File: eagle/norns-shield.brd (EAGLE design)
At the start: 85.1 x 80 mm, 80 parts, among them J1 TRS-IN, J2 TRS-OUT, J3 ISP-ROW, Q1 ASFL-12.288mhz, SW1 PVA1, SW2 PVA1, SW3 PVA1, U1 CS4270, X1 RASPI_BOARD_B+#_E3

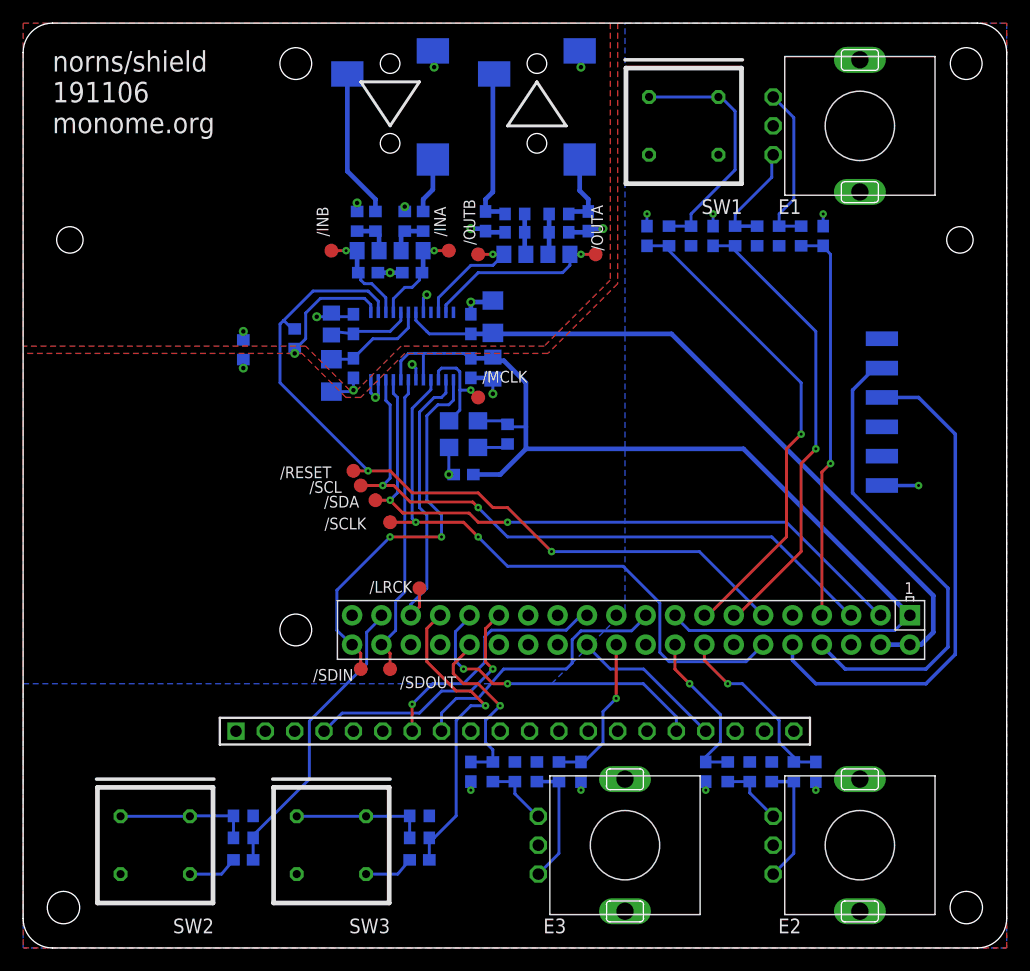
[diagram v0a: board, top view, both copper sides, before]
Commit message: Flip Tip and Ring on IO jacks.
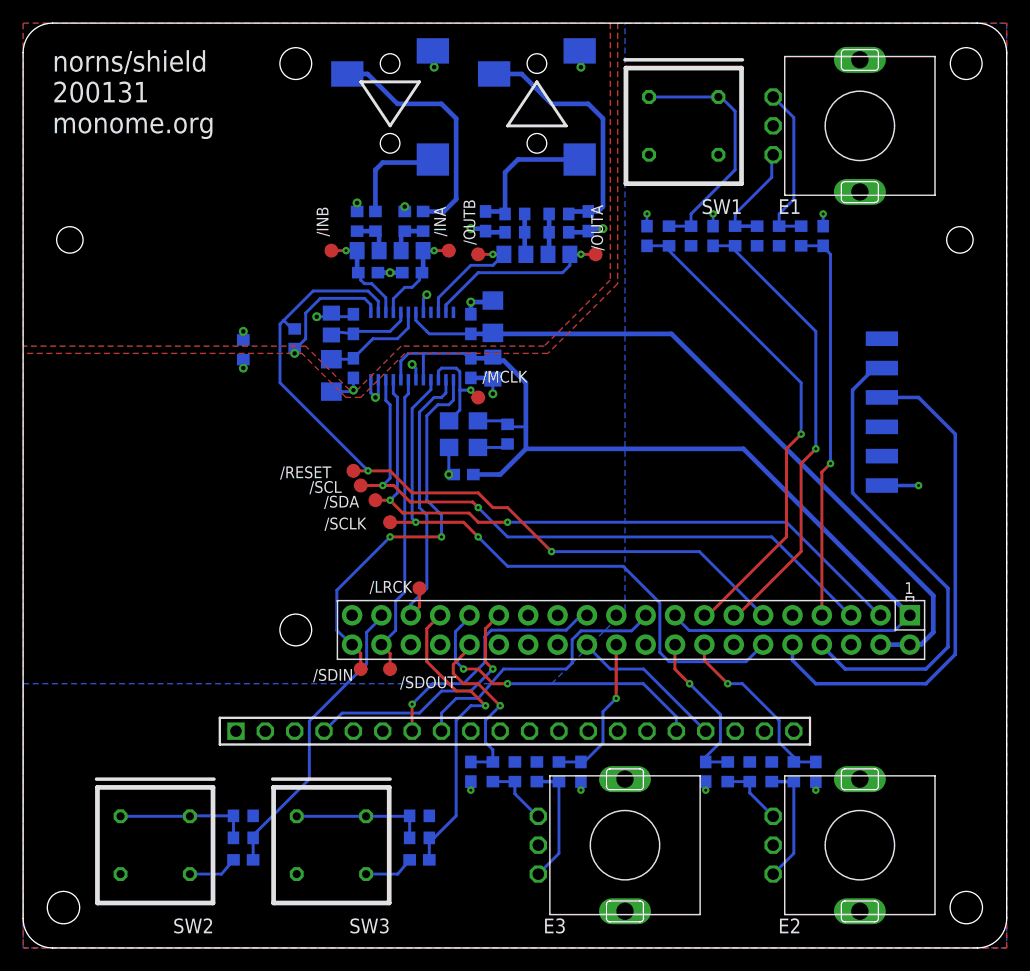
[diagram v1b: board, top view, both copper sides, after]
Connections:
- removed net N$11: J1.2, R7.2
- removed net N$12: J1.3, R9.2
- new net N$7: J1.2, R9.2
- new net N$8: J1.3, R7.2
- net N$15: now also J2.3; no longer J2.2
- net N$16: now also J2.2; no longer J2.3
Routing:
- net N$8: track 0.00 -> 21.3 mm
- net N$15: track 6.58 -> 22.2 mm
- net N$12: track 12.9 -> 0.00 mm
- net N$7: track 0.00 -> 8.94 mm
- net N$11: track 4.84 -> 0.00 mm
- net N$16: track 14.0 -> 12.6 mm
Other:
- board text added: "norns/shield 200131 monome.org"
- board text removed: "norns/shield 191106 monome.org"
